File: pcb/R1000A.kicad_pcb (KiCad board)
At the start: 4 copper layers, 175 x 65.5 mm, 127 parts, among them J01 PCIESOCKET-X1, J02 PCIESOCKET-X1, J03 PCIESOCKET-X1, J04 PCIESOCKET-X1, J05 PCIESOCKET-X1, J06 PCIESOCKET-X1, J07 PCIESOCKET-X1, J08 PCIESOCKET-X1, J09 PCIESOCKET-X1, J10 PCIESOCKET-X1, J11 PCIESOCKET-X1, J12 PCIESOCKET-X1, J13 PCIESOCKET-X1, J14 PCIESOCKET-X1, J15 PCIESOCKET-X1, J17 USB_B_RECEPTACLE, J2 CONN127P-02X05, J25 SOCKET420P-02X04-CPU, J31 USB_A_RECEPTACLE_2, J81 SOCKET254P-01X02, J82 SOCKET254P-01X02, J83 CONN_01X03, Q1 DMG2305UX-7, Q2 PSMN1R2-30YLC, Q3 Q_PNP_BEC, Q4 Q_NPN_BEC, Q5 Q_PNP_BEC, Q6 Q_PNP_BEC, U1 LPC1769FBD100,551, U2 AP3418, U20 M24C08-WDW6TP, U3 BD9E302EFJ-E2, U4 INA3221AIRGVR, U5 LM5060MM/NOPB, Y1 XTAL4_12MHz

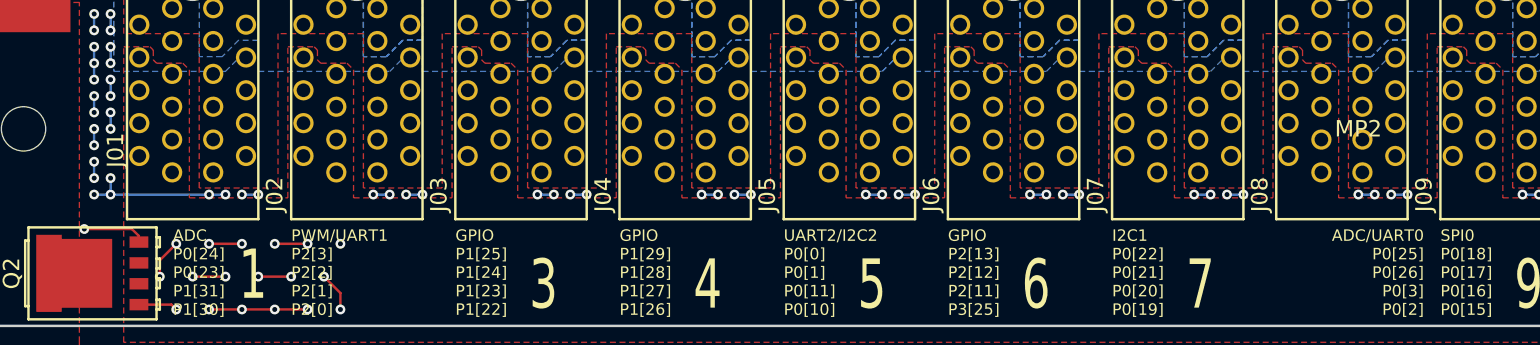
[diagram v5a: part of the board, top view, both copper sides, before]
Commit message: wip, need to correct footprints
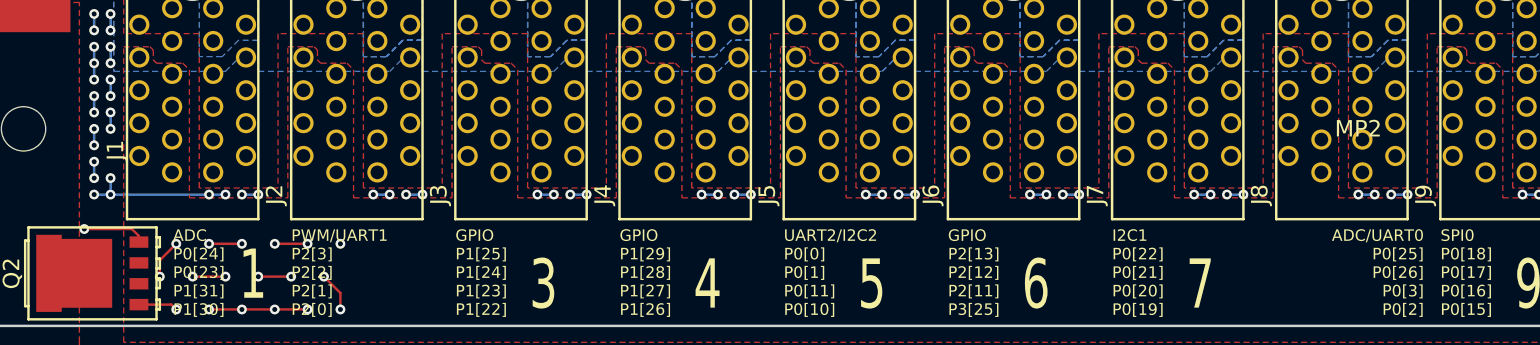
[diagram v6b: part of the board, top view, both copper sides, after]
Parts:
- renumbered J01 to J1, J2 to J16, J02 to J2, J03 to J3, J04 to J4, J05 to J5, J06 to J6, J07 to J7, J08 to J8, J09 to J9
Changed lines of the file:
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@@
-(kicad_pcb (version 4) (host pcbnew 4.0.3+e1-6302~38~ubuntu14.04.1-stable)
+(kicad_pcb (version 4) (host pcbnew 4.0.6-e0-6349~53~ubuntu14.04.1)
   (general
     (links 726)
     (no_connects 502)
-    (area 50.924999 73.424999 226.075001 139.075001)
+    (area 47.4 63.678571 240.500001 155.325)
     (thickness 1.6)
     (drawings 71)
@@
   (module Main:PCIESOCKET-X1 (layer F.Cu)
     (at 150 120 90)
-    (fp_text reference J09 (at -11 -5 270) (layer F.SilkS)
+    (fp_text reference J9 (at -11 -5 90) (layer F.SilkS)
       (effects (font (size 1 1) (thickness 0.15)))
     )
@@
   (module Main:PCIESOCKET-X1 (layer F.Cu)
     (at 140 120 90)
-    (fp_text reference J08 (at -11 -5 270) (layer F.SilkS)
+    (fp_text reference J8 (at -11 -5 90) (layer F.SilkS)
       (effects (font (size 1 1) (thickness 0.15)))
     )
@@
   (module Main:PCIESOCKET-X1 (layer F.Cu)
     (at 130 120 90)
-    (fp_text reference J07 (at -11 -5 270) (layer F.SilkS)
+    (fp_text reference J7 (at -11 -5 90) (layer F.SilkS)
       (effects (font (size 1 1) (thickness 0.15)))
     )
@@
   (module Main:PCIESOCKET-X1 (layer F.Cu)
     (at 120 120 90)
-    (fp_text reference J06 (at -11 -5 270) (layer F.SilkS)
+    (fp_text reference J6 (at -11 -5 90) (layer F.SilkS)
       (effects (font (size 1 1) (thickness 0.15)))
     )
@@
   (module Main:PCIESOCKET-X1 (layer F.Cu)
     (at 110 120 90)
-    (fp_text reference J05 (at -11 -5 270) (layer F.SilkS)
+    (fp_text reference J5 (at -11 -5 90) (layer F.SilkS)
       (effects (font (size 1 1) (thickness 0.15)))
     )
@@
   (module Main:PCIESOCKET-X1 (layer F.Cu)
     (at 100 120 90)
-    (fp_text reference J04 (at -11 -5 270) (layer F.SilkS)
+    (fp_text reference J4 (at -11 -5 90) (layer F.SilkS)
       (effects (font (size 1 1) (thickness 0.15)))
     )
@@
   (module Main:PCIESOCKET-X1 (layer F.Cu)
     (at 90 120 90)
-    (fp_text reference J03 (at -11 -5 270) (layer F.SilkS)
+    (fp_text reference J3 (at -11 -5 90) (layer F.SilkS)
       (effects (font (size 1 1) (thickness 0.15)))
     )
@@
   (module Main:PCIESOCKET-X1 (layer F.Cu)
     (at 80 120 90)
-    (fp_text reference J02 (at -11 -5 270) (layer F.SilkS)
+    (fp_text reference J2 (at -11 -5 90) (layer F.SilkS)
       (effects (font (size 1 1) (thickness 0.15)))
     )
@@
   (module Main:PCIESOCKET-X1 (layer F.Cu)
     (at 70 120 90)
-    (fp_text reference J01 (at -8.3 -4.7 270) (layer F.SilkS)
+    (fp_text reference J1 (at -8.3 -4.7 90) (layer F.SilkS)
       (effects (font (size 1 1) (thickness 0.15)))
     )
@@
   (module Main:CONN127P-02X05 (layer F.Cu)
     (at 103.5 77.7 270)
-    (fp_text reference J2 (at -2.2 -2.7 270) (layer F.SilkS) hide
+    (fp_text reference J16 (at -2.2 -2.7 270) (layer F.SilkS) hide
       (effects (font (size 1 1) (thickness 0.15)))
     )

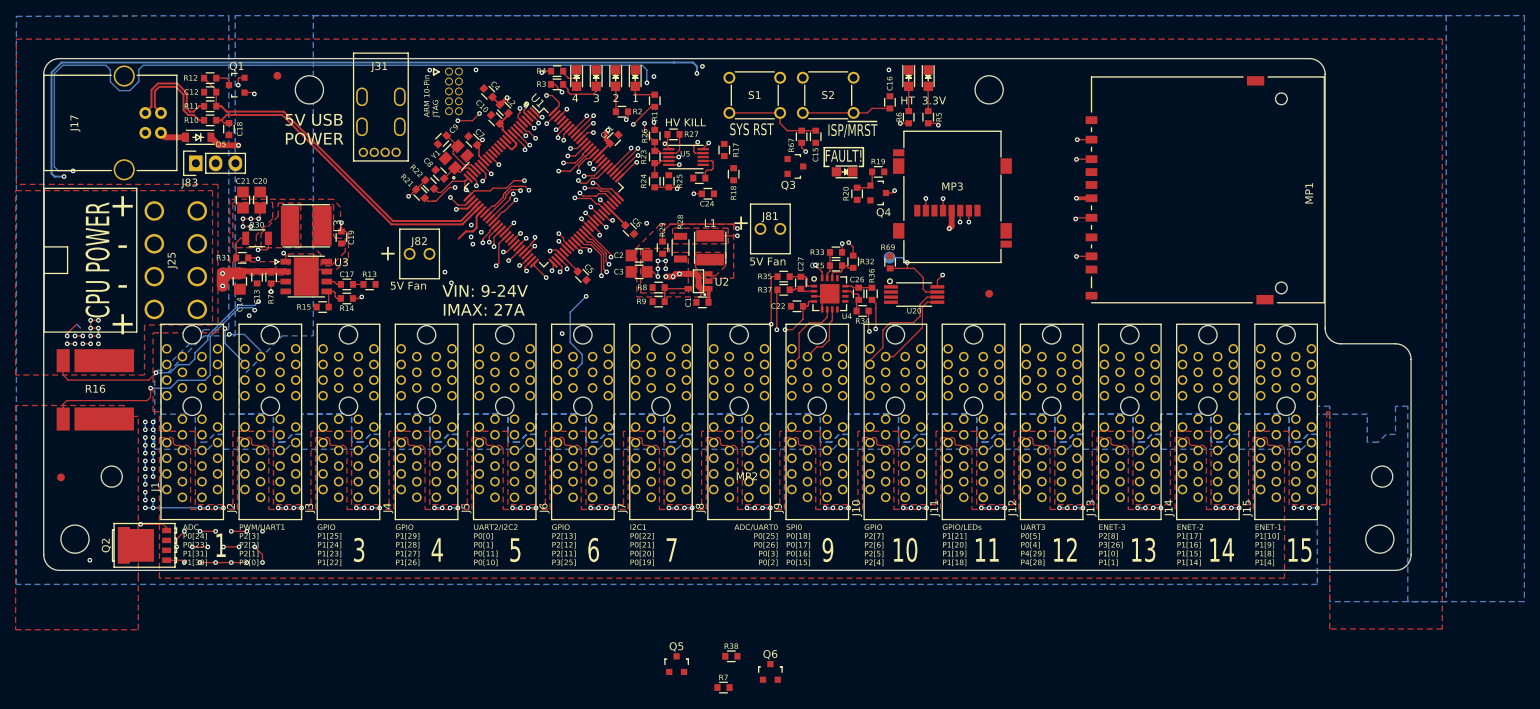
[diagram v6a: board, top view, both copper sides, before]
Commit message: completed schematics, layout is clean
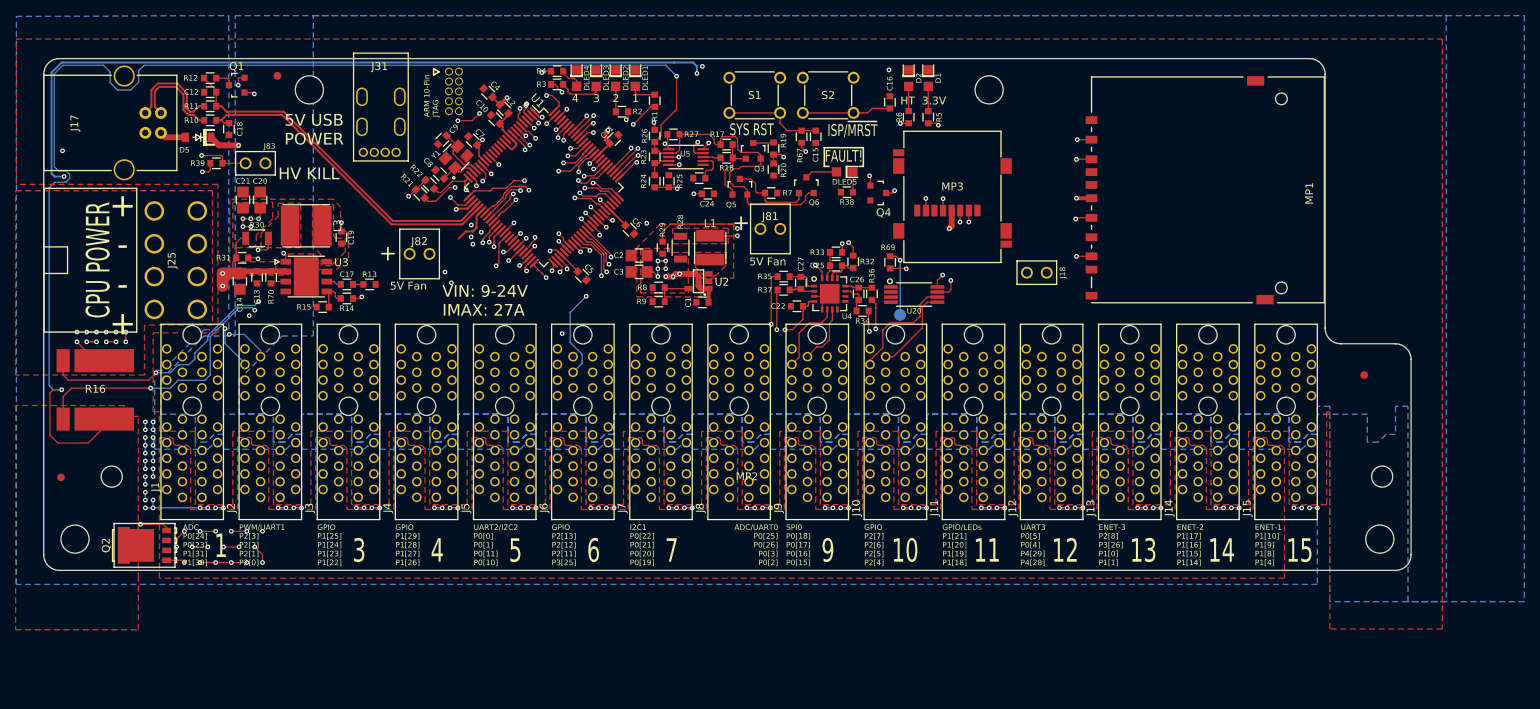
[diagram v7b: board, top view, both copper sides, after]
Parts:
- added J18: SOCKET254P-01X02, Main:SOCKET254P-01X02_2, F.Cu at (178.1, 100.9)
- added R39: RC0603FR-0766K5L, Main:RESC0603, F.Cu at (73.1, 86.9)
- C23: value CC0603JRNPO9BN102 -> CC0603KRX7R9BB104
- D1: value Led_Small -> LTST-C171GKT; footprint Main:LED-0805 -> Main:DIOC200X120X110
- D2: value Led_Small -> LTST-C171TBKT; footprint Main:LED-0805 -> Main:DIOC200X120X110
- D5: value D_Schottky_Small -> MBR0520LT1G
- DLED1, DLED2, DLED3, DLED4: value Led_Small -> LTW-170TK; footprint Main:LED-0805 -> Main:DIOC200X120X110
- DLED5: value Led_Small -> LTST-C171KRKT; footprint Main:LED-0805 -> Main:DIOC200X120X110
- J83: value CONN_01X03 -> SOCKET254P-01X02; footprint Main:SOCKET254P-01X03 -> Main:SOCKET254P-01X02_2
- U20: value M24C08-WDW6TP -> M24C08-FDW6TP
- moved R7 63.6 mm to (144.1, 90.7)
- moved Q6 62.5 mm to (148.6, 89.7)
- moved Q5 61.6 mm to (140.1, 89.9)
- moved R38 61.2 mm to (153.8, 90.6), turned to 180 degrees
- moved FID3 49.1 mm to (220.0, 114.0)
- moved R19 13.7 mm to (144.4, 85.0), turned to 270 degrees
- moved R20 11.1 mm to (144.4, 87.7)
- moved TP1 7.45 mm to (160.6, 106.3)
- moved Q3 5.76 mm to (141.8, 85.3), turned to 0 degrees
- moved J83 5.10 mm to (78.1, 86.9)
- moved R18 2.28 mm to (138.4, 86.2), turned to 180 degrees
- moved R17 0.76 mm to (138.4, 84.5), turned to 0 degrees
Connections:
- net CHIP_~PGD renamed /PowerMonitor/LM5060_~PGD
- J1 pad B12: (no net) -> GND
- J1 pad B13: (no net) -> GND
- J1 pad B14: (no net) -> GND
- J1 pad B15: (no net) -> GND
- J25 pad 8: HV_EN -> /HV_EN_CONN
- J83 pad 2: LV_EN -> GND
- R69 pad 1: GND -> /EE_~WC
- R69 pad 2: Net-(R69-Pad2) -> +3V3
- TP1 pad 1: Net-(R69-Pad2) -> /EE_~WC
- U20 pad 7: Net-(R69-Pad2) -> /EE_~WC
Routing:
- net PFET_D: track 20.5 -> 202.2 mm, vias 1 -> 2
- net /EE_~WC: track 0.00 -> 32.4 mm, vias 0 -> 2
- net LV_EN: track 23.9 -> 1.97 mm, vias 1 -> 0
- net HT_IN: track 3.72 -> 22.0 mm, vias 0 -> 12
- net (no net): track 15.7 -> 0.00 mm, vias 14 -> 0
- net Net-(Q4-Pad1): track 3.66 -> 17.5 mm, vias 0 -> 2
- net HV_EN: track 143.7 -> 130.2 mm, vias 5 -> 4
- net Net-(R69-Pad2): track 11.5 -> 0.00 mm, vias 1 -> 0
- net Net-(Q5-Pad3): track 0.00 -> 11.0 mm
- net HT: track 390.2 -> 379.8 mm, vias 26 -> 24
- net Net-(Q3-Pad1): track 0.00 -> 9.27 mm
- net /HV_EN_CONN: track 0.00 -> 7.67 mm, vias 0 -> 1
- net Net-(DLED5-Pad2): track 0.00 -> 4.14 mm
- net Net-(Q3-Pad3): track 0.00 -> 2.63 mm
- net Net-(DLED5-Pad1): track 0.00 -> 2.61 mm
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
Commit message: generated gerbers for review
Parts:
- added A1: ART, Symbols:KiCad-Logo2_12mm_SilkScreen, B.Cu at (191.8, 85.3)
- added A2: ART, pluggee:pluggeeLabsLogo, B.Cu at (114.6, 89.0)
- added A3: ART, Symbols:OSHW-Logo_11.4x12mm_SilkScreen, B.Cu at (199.3, 99.1)
- added A4: ART, Symbols:Symbol_GNU-Logo_SilkscreenTop, B.Cu at (185.6, 98.3)
- moved TP1 7.16 mm to (159.1, 99.3)
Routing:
- net HT_IN: track 22.0 -> 127.3 mm
- net HT: track 379.8 -> 365.9 mm
- net /EE_~WC: track 32.4 -> 26.9 mm
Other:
- board text added: "JuicyBoard - R1000AX v1.3 Designed by plugg.ee Labs LLC San Jose CA, USA http://plugg.ee"
- board text removed: "JuicyBoard R1000A v1.2.0 - 12/2016 http://plugg.ee Designed by plugg.ee Labs, CA, USA"
